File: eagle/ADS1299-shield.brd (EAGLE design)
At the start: 101.6 x 53.3 mm, 125 parts, among them IC1 ADS1299IPAG, IC2 TPS72325DBVT, IC3 TPS73225DBVT, IC5 24AA256UID, IC6 TPS604XXDBV, IC7 OPA376DBV, IC8 OPA376DBV, J8 Electrode Connector, U2 TXB0108PWR, U3 TXB0108PWR

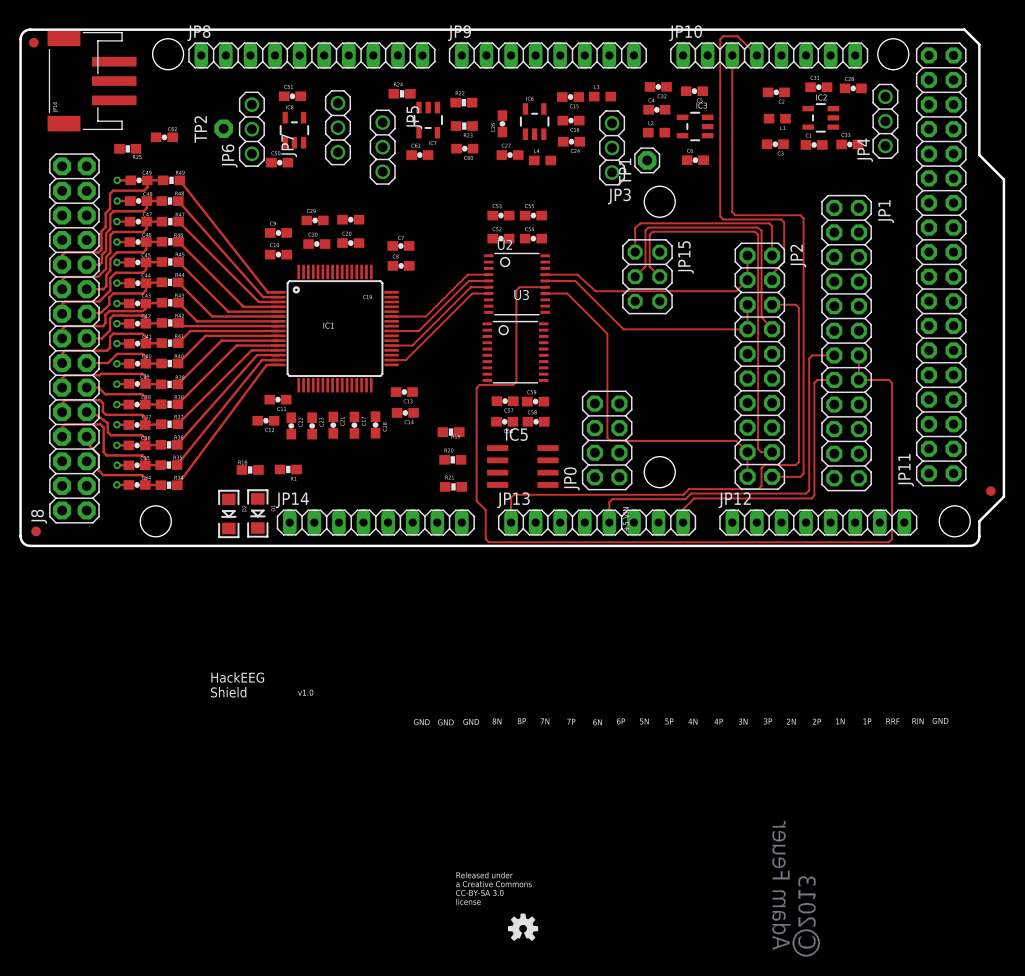
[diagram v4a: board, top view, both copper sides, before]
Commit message: routed more AGND and AVDD signals to use AVDD and AGND layers
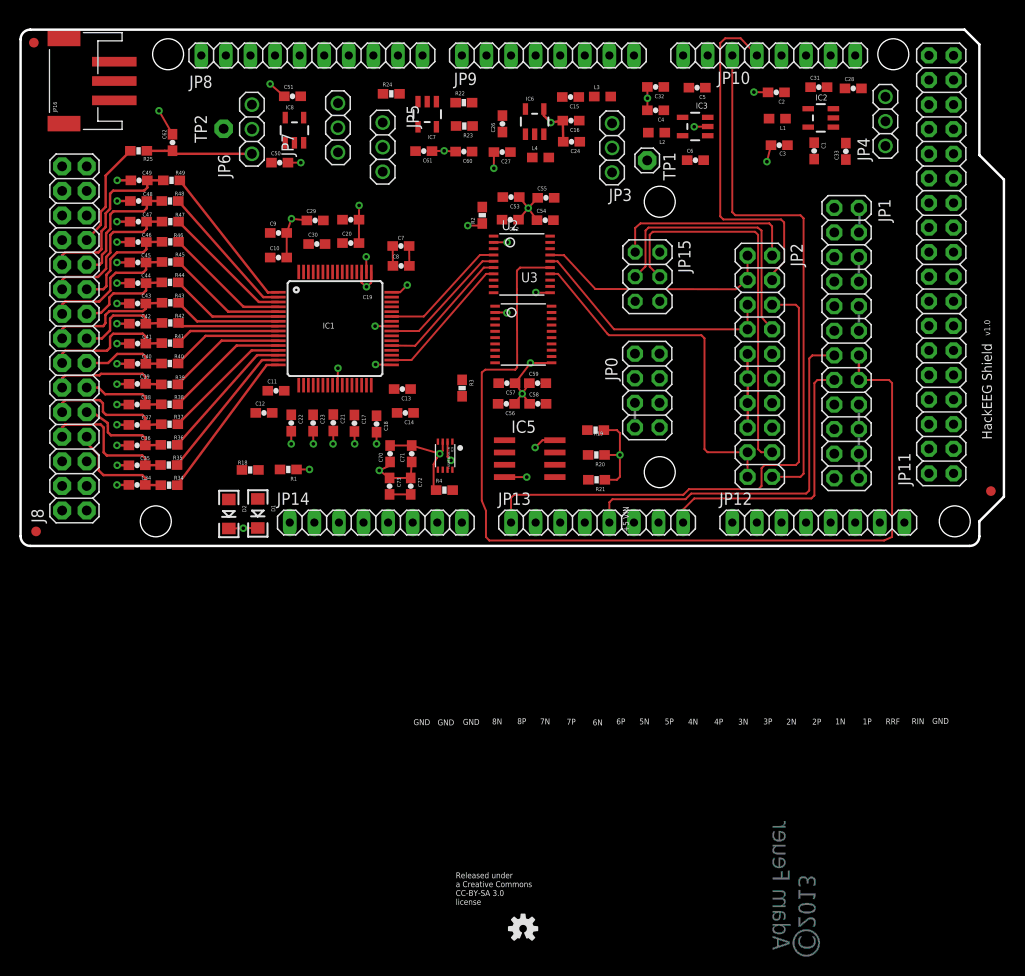
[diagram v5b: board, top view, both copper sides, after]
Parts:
- added C70, C72: 1uF, SparkFun-Passives:0603-CAP
- added C71, C73: 0.1uF, SparkFun-Passives:0603-CAP
- added IC9: TXS0102DCTR, adafruit:VFSOP-8
- added R2, R3, R4: 10k, SparkFun-Passives:0603-RES
- moved R19 14.9 mm to (59.5, 12.1)
- moved R20 14.8 mm to (59.6, 9.53), turned to 180 degrees
- moved R21 14.8 mm to (59.6, 6.96), turned to 180 degrees
- moved JP0 6.61 mm to (64.9, 16.2)
- moved C54 2.26 mm to (54.3, 33.8)
- moved C55 2.24 mm to (54.4, 36.1)
- moved C52 2.18 mm to (50.7, 33.8), turned to 180 degrees
- moved C53 2.17 mm to (50.8, 36.2), turned to 180 degrees
- moved U2 2.09 mm to (51.9, 29.2)
- moved U3 2.00 mm to (52.1, 22.0)
- moved C59 1.92 mm to (53.5, 16.9)
- moved C57 1.86 mm to (50.4, 16.9)
- moved C58 1.86 mm to (53.6, 14.8)
- moved C56 1.86 mm to (50.3, 14.8)
- moved R25 1.14 mm to (12.3, 40.9)
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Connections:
- removed net GND: C7.2, C8.2, JP16.1
- new net N$37: IC9.P$6, R4.2
- new net N$561: R2.2, U2.10
- new net N$562: R3.2, U3.10
- net AGND: now also C70.1, C71.1, C72.1, C73.1, IC9.P$2, JP16.1, U3.16, U3.17, U3.4, U3.5
- net AVSS: now also C7.2, C8.2
- net DVDD: now also C70.2, C71.2, IC9.P$3, R2.1, R3.1, R4.1; no longer U2.10, U3.10
- net IOREF: now also C72.2, C73.2, IC9.P$7
- net SCL: now also IC9.P$4; no longer U3.4
- net SCL1: now also IC9.P$1; no longer U3.17
- net SDA: now also IC9.P$5; no longer U3.5
- net SDA1: now also IC9.P$8; no longer U3.16
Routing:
- net AGND: track 52.5 -> 349.5 mm, vias 16 -> 46
- net DVDD: track 0.00 -> 94.2 mm, vias 0 -> 8
- net N$105: track 0.00 -> 11.1 mm
- net REF_ELEC: track 0.00 -> 11.0 mm
- net !ADS_SPI_CS: track 0.00 -> 7.76 mm
- net ADS_DRDY: track 0.00 -> 7.62 mm
- net !ADS_PWDN: track 0.00 -> 2.67 mm
- net !ADS_RESET: track 0.00 -> 2.54 mm
- net ADS_START: track 0.00 -> 2.54 mm
- net IOREF: track 0.00 -> 2.18 mm
- net AVSS: track 0.00 -> 2.06 mm
- net AVDD: track 0.00 -> 2.06 mm
- net SPI_IN: track 12.9 -> 14.6 mm
- net CLK: track 12.5 -> 14.2 mm
- net SPI_CLK: track 12.2 -> 13.7 mm
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
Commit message: routed I2C signals to EEPROM level shifter - to prevent them from going under the AIN block
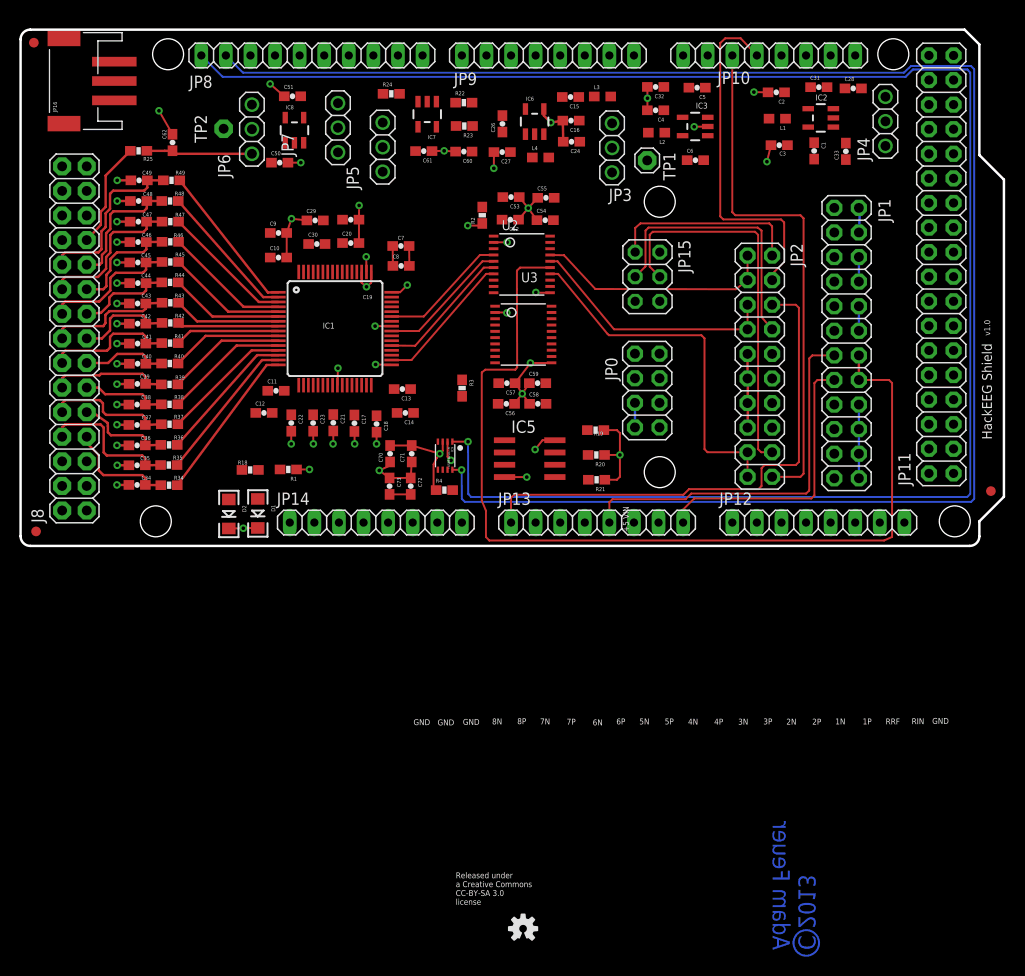
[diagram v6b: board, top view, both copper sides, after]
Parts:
- turned JP5 to 90 degrees
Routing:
- net SCL1: track 0.00 -> 183.5 mm, vias 0 -> 1
- net SDA1: track 0.00 -> 180.0 mm, vias 0 -> 1
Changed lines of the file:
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@@
 <attribute name="VALUE" x="42.799" y="42.0624" size="0.4064" layer="27" font="vector" rot="R180"/>
 </element>
-<element name="JP5" library="adafruit" package="1X03" value="SRB1-BIAS" x="37.5412" y="41.3258" smashed="yes" rot="R270">
-<attribute name="NAME" x="40.005" y="45.6946" size="1.27" layer="25" font="vector" ratio="10" rot="R270"/>
-<attribute name="VALUE" x="34.3662" y="45.1358" size="1.27" layer="27" rot="R270"/>
+<element name="JP5" library="adafruit" package="1X03" value="SRB1-BIAS" x="37.5412" y="41.3258" smashed="yes" rot="R90">
+<attribute name="NAME" x="35.0774" y="36.957" size="1.27" layer="25" font="vector" ratio="10" rot="R90"/>
+<attribute name="VALUE" x="40.7162" y="37.5158" size="1.27" layer="27" rot="R90"/>
 </element>
 <element name="R22" library="SparkFun-Passives" package="0603-RES" value="2M" x="45.9232" y="45.9232" smashed="yes">
@@
 <wire x1="47.498" y1="27.0764" x2="50.3682" y2="24.2062" width="0.2032" layer="15"/>
 <wire x1="55.3304" y1="11.049" x2="54.0512" y2="11.049" width="0.2032" layer="1"/>
-<wire x1="54.0512" y1="11.049" x2="53.2892" y2="10.287" width="0.2032" layer="1"/>
-<via x="53.2892" y="10.287" extent="1-16" drill="0.381"/>
-<wire x1="53.2892" y1="10.287" x2="44.069" y2="10.287" width="0.2032" layer="15"/>
-<wire x1="44.069" y1="10.287" x2="43.434" y2="9.652" width="0.2032" layer="15"/>
+<wire x1="54.0512" y1="11.049" x2="53.2892" y2="10.0838" width="0.2032" layer="1"/>
+<via x="53.2892" y="10.0838" extent="1-16" drill="0.381"/>
+<wire x1="53.2892" y1="10.0838" x2="44.1706" y2="10.0838" width="0.2032" layer="15"/>
+<wire x1="44.1706" y1="10.0838" x2="43.434" y2="9.652" width="0.2032" layer="15"/>
 <wire x1="35.8636" y1="28.4306" x2="35.8394" y2="29.9974" width="0.2032" layer="1"/>
 <via x="35.8394" y="29.9974" extent="1-16" drill="0.381"/>
@@
 <contactref element="IC7" pad="4"/>
 <wire x1="41.1886" y1="43.4293" x2="43.0886" y2="46.0295" width="0" layer="19" extent="1-1"/>
-<wire x1="37.5412" y1="38.7858" x2="41.1886" y2="43.4293" width="0" layer="19" extent="1-1"/>
+<wire x1="37.5412" y1="43.8658" x2="41.1886" y2="43.4293" width="0" layer="19" extent="1-1"/>
 </signal>
 <signal name="N$105">
@@
 <contactref element="JP5" pad="1"/>
 <contactref element="IC1" pad="62"/>
-<wire x1="37.5412" y1="43.8658" x2="39.2802" y2="46.8376" width="0" layer="19" extent="1-1"/>
-<wire x1="29.8636" y1="28.4306" x2="37.5412" y2="43.8658" width="0" layer="19" extent="1-1"/>
+<wire x1="37.5412" y1="38.7858" x2="39.2802" y2="46.8376" width="0" layer="19" extent="1-1"/>
+<wire x1="29.8636" y1="28.4306" x2="37.5412" y2="38.7858" width="0" layer="19" extent="1-1"/>
 </signal>
 <signal name="N$19">
@@
 <contactref element="JP8" pad="1"/>
 <contactref element="IC9" pad="P$1"/>
-<wire x1="44.7428" y1="10.8988" x2="18.796" y2="50.8" width="0" layer="19" extent="1-1"/>
+<wire x1="18.796" y1="50.8" x2="21.0058" y2="48.5902" width="0.2032" layer="16"/>
+<wire x1="21.0058" y1="48.5902" x2="91.567" y2="48.5902" width="0.2032" layer="16"/>
+<wire x1="91.567" y1="48.5902" x2="92.329" y2="49.3522" width="0.2032" layer="16"/>
+<wire x1="92.329" y1="49.3522" x2="97.9551" y2="49.3522" width="0.2032" layer="16"/>
+<wire x1="97.9551" y1="49.3522" x2="98.2472" y2="49.0093" width="0.2032" layer="16"/>
+<wire x1="98.2472" y1="49.0093" x2="98.2472" y2="5.4991" width="0.2032" layer="16"/>
+<wire x1="98.2472" y1="5.4991" x2="97.9297" y2="5.1816" width="0.2032" layer="16"/>
+<wire x1="97.9297" y1="5.1816" x2="46.6725" y2="5.1816" width="0.2032" layer="16"/>
+<wire x1="46.6725" y1="5.1816" x2="46.3804" y2="5.4991" width="0.2032" layer="16"/>
+<wire x1="46.3804" y1="5.4991" x2="46.355" y2="10.8966" width="0.2032" layer="16"/>
+<via x="46.355" y="10.8966" extent="1-16" drill="0.381"/>
+<wire x1="46.355" y1="10.8966" x2="46.2004" y2="10.8988" width="0.2032" layer="1"/>
+<wire x1="46.2004" y1="10.8988" x2="44.7428" y2="10.8988" width="0.2032" layer="1"/>
 </signal>
 <signal name="SDA1">
 <contactref element="JP8" pad="2"/>
 <contactref element="IC9" pad="P$8"/>
-<wire x1="44.7428" y1="7.9988" x2="21.336" y2="50.8" width="0" layer="19" extent="1-1"/>
+<wire x1="21.336" y1="50.8" x2="23.114" y2="49.022" width="0.2032" layer="16"/>
+<wire x1="23.114" y1="49.022" x2="91.3892" y2="49.022" width="0.2032" layer="16"/>
+<wire x1="91.3892" y1="49.022" x2="92.1258" y2="49.7078" width="0.2032" layer="16"/>
+<wire x1="92.1258" y1="49.7078" x2="98.3361" y2="49.7078" width="0.2032" layer="16"/>
+<wire x1="98.3361" y1="49.7078" x2="98.6536" y2="49.3649" width="0.2032" layer="16"/>
+<wire x1="98.6536" y1="49.3649" x2="98.6536" y2="4.9911" width="0.2032" layer="16"/>
+<wire x1="98.6536" y1="4.9911" x2="98.3361" y2="4.6736" width="0.2032" layer="16"/>
+<wire x1="98.3361" y1="4.6736" x2="46.0375" y2="4.6736" width="0.2032" layer="16"/>
+<wire x1="46.0375" y1="4.6736" x2="45.72" y2="4.9911" width="0.2032" layer="16"/>
+<wire x1="45.72" y1="4.9911" x2="45.6946" y2="7.9756" width="0.2032" layer="16"/>
+<via x="45.6946" y="7.9756" extent="1-16" drill="0.381"/>
+<wire x1="45.6946" y1="7.9756" x2="44.7428" y2="7.9988" width="0.2032" layer="1"/>
 </signal>
 <signal name="SCL">

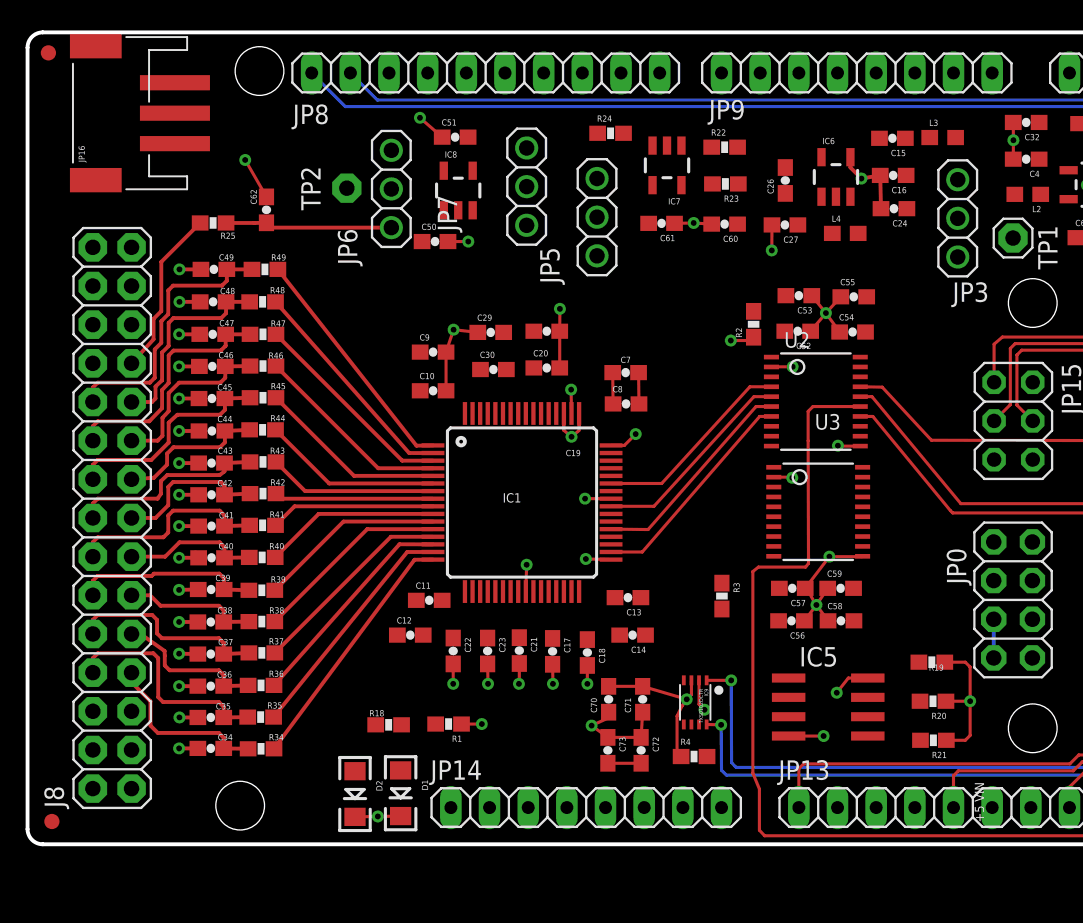
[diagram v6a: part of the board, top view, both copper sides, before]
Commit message: routed JST connector signals - ADS_CLK, ADS_START, AGND
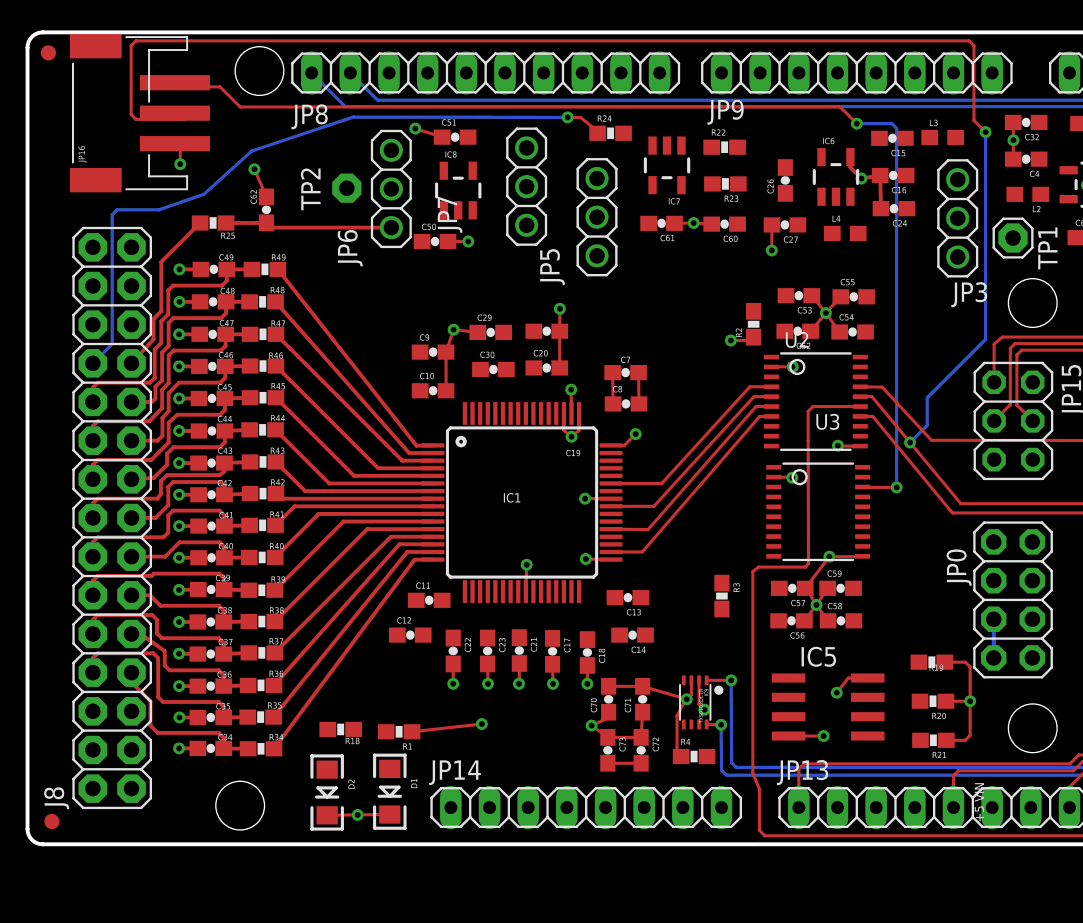
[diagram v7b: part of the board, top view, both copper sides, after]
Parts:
- moved R1 3.29 mm to (24.5, 7.52)
- moved R18 3.16 mm to (20.7, 7.67), turned to 180 degrees
- moved D2 1.83 mm to (19.8, 3.53)
- moved D1 0.72 mm to (23.9, 3.58)
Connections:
- net N$105 renamed REF_ELEC_CON
- net N$106 renamed BIAS_ELEC_CON
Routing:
- net ADS_SPI_CLK: track 26.2 -> 119.4 mm, vias 0 -> 2
- net ADS_START: track 2.54 -> 77.0 mm, vias 0 -> 2
- net BIAS_ELEC_CON: track 0.00 -> 44.4 mm, vias 0 -> 1
- net AGND: track 349.5 -> 355.9 mm, vias 46 -> 47
- net DVDD: track 94.2 -> 97.5 mm
